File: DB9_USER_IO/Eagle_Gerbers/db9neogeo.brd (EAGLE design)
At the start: 81.5 x 22.7 mm, 14 parts, among them IC1 74HC597D, IC2 74HC597D, IC3 74HC597D

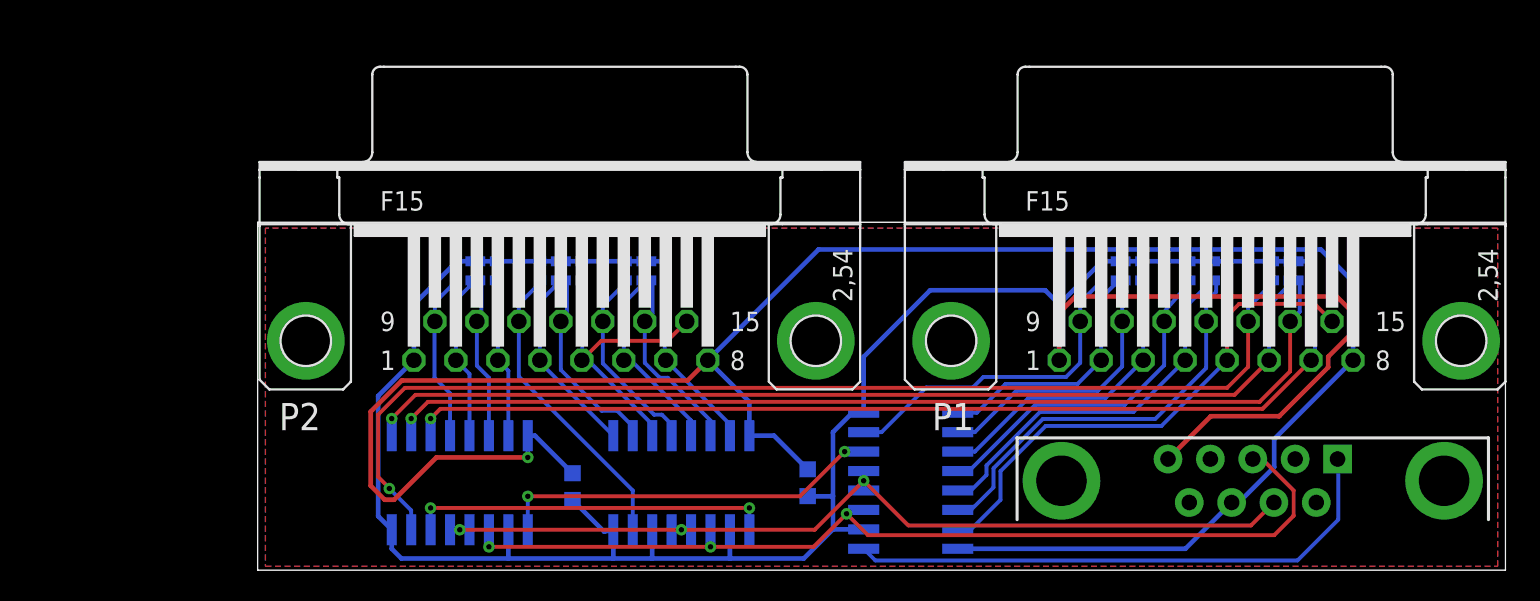
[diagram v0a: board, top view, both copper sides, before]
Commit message: updated db9neogeo with usb3 input. added db9neogeo
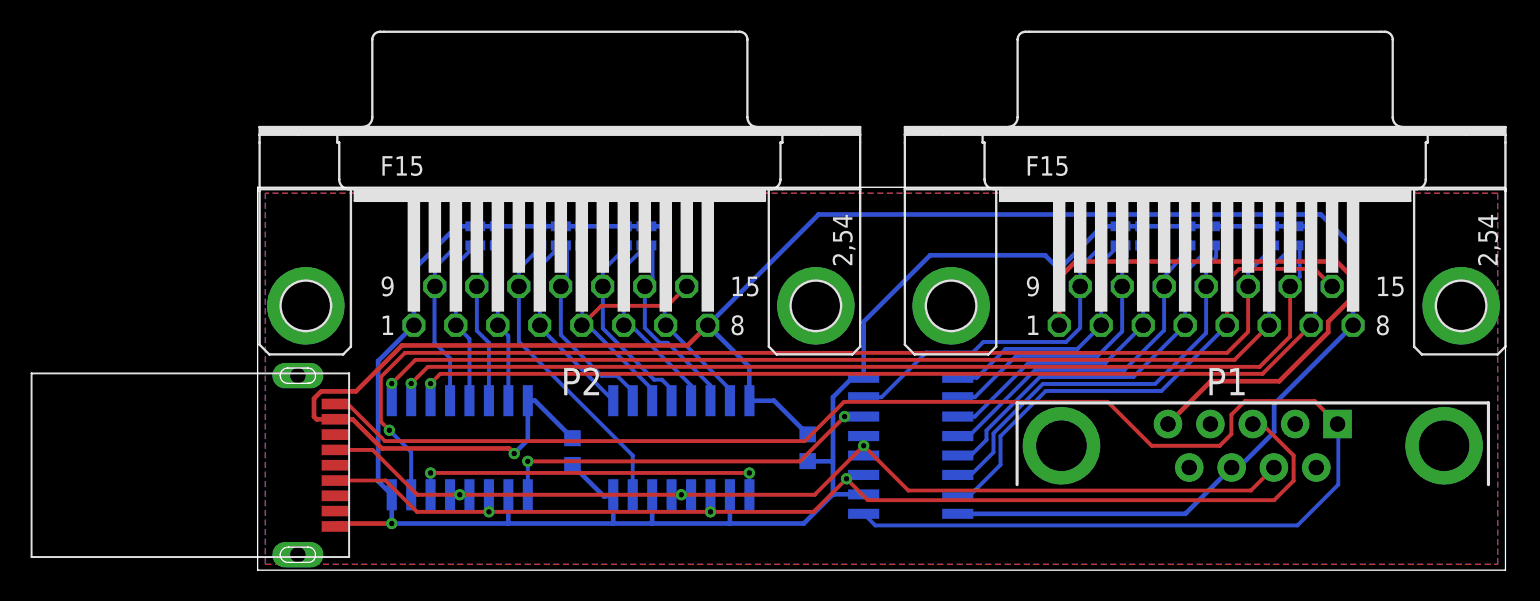
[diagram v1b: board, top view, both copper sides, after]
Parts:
- added K2: 692112030100, Wuerth_Elektronik_eiCan_Communication_Connectors_STENCIL:692112030100
- moved RN1 2.29 mm to (56.4, 21.8)
- moved RN2 2.29 mm to (14.2, 21.8)
- moved RN3 2.29 mm to (25.4, 21.8)
- moved RN4 2.29 mm to (19.8, 21.8)
- moved RN5 2.29 mm to (62.2, 21.8)
- moved RN6 2.29 mm to (67.7, 21.8)
- moved IC1 2.29 mm to (42.7, 8.13)
- moved J1 2.29 mm to (65.0, 8.13)
- moved C1 2.29 mm to (35.9, 8.00)
- moved C2 2.29 mm to (20.6, 7.75)
- moved IC2 2.29 mm to (13.2, 8.00)
- moved IC3 2.29 mm to (27.7, 8.00)
- moved P1 2.29 mm to (62.0, 17.3)
- moved P2 2.29 mm to (19.8, 17.3)
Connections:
- net CLK: now also K2.2
- net DAT: now also K2.5
- net GND: now also K2.4
- net LAT: now also K2.3
- net VCC: now also K2.9
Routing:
- net DAT: track 36.4 -> 107.7 mm
- net CLK: track 63.2 -> 74.1 mm
- net LAT: track 60.7 -> 70.0 mm
- net GND: track 139.3 -> 144.7 mm
- net VCC: track 168.7 -> 172.8 mm, vias 0 -> 1
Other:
- board size 81.5 x 22.7 mm -> 81.5 x 25 mm
- board text added: "P1"
- board text added: "P2"
